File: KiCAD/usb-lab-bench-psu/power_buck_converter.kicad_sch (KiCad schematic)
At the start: 15 parts, among them U10 LMR16006X

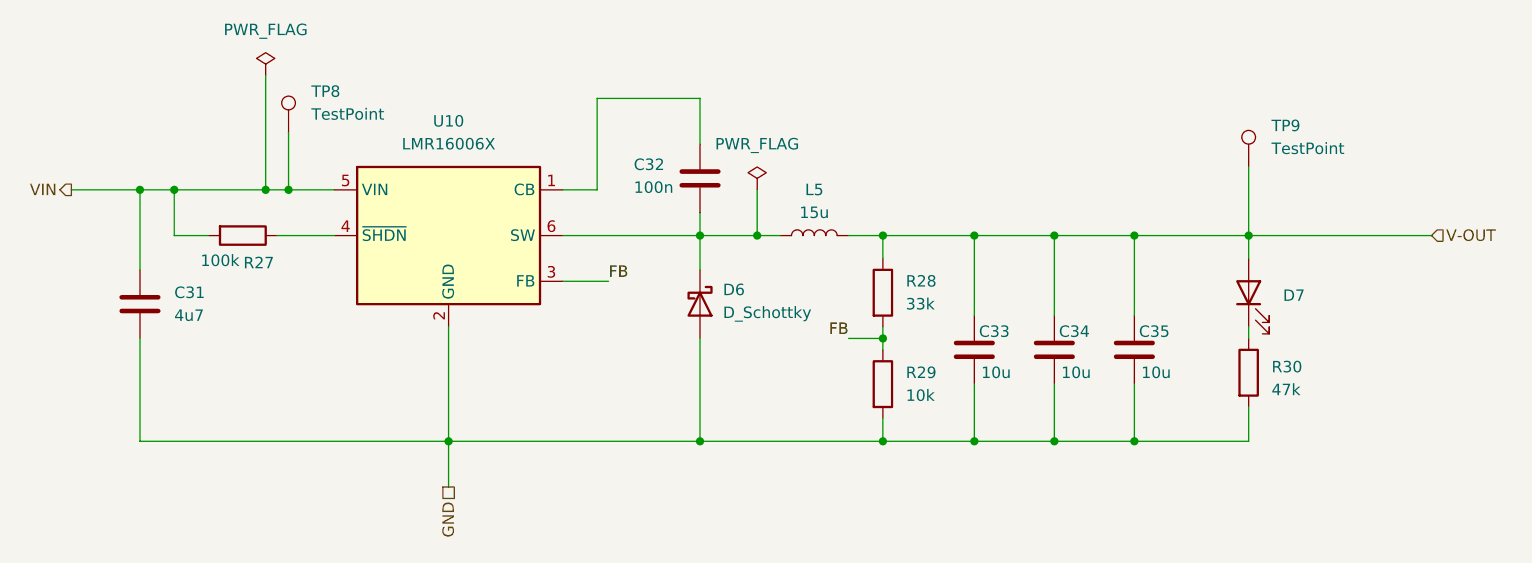
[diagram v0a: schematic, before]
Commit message: Fixed label directions
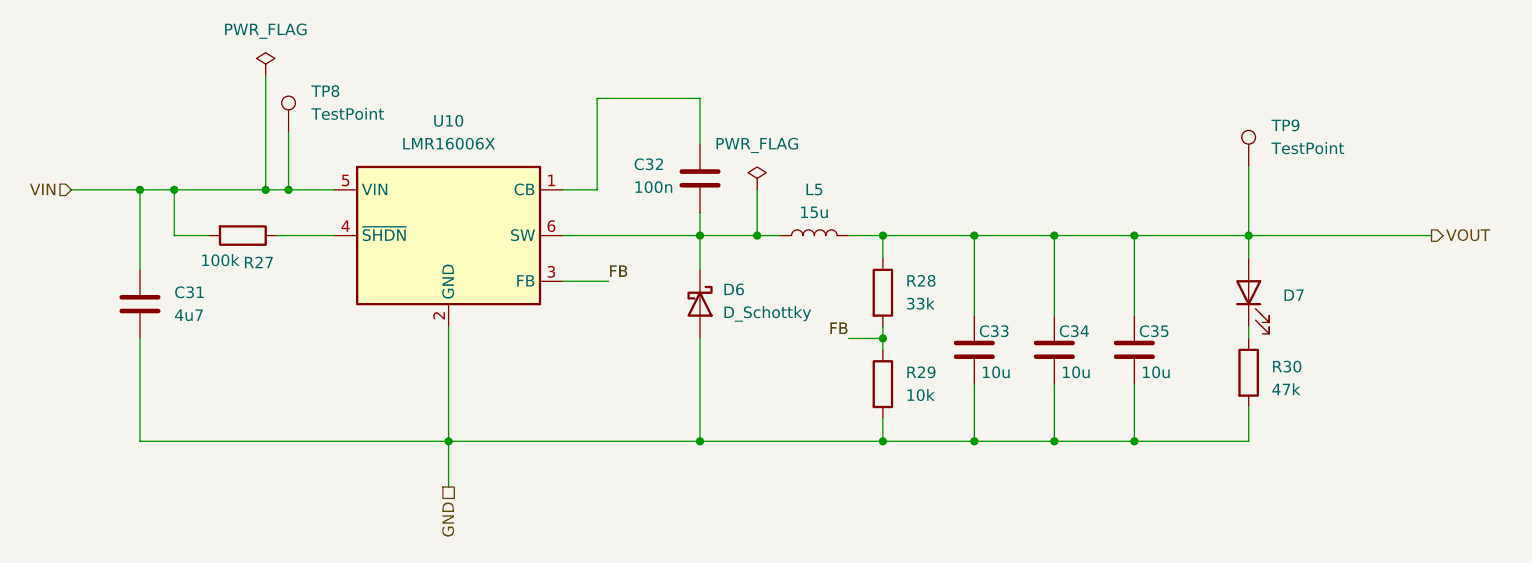
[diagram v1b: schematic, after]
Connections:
- net V-OUT renamed VOUT
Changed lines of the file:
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@@
 	)
 	(hierarchical_label "VIN"
-		(shape output)
+		(shape input)
 		(at 59.69 71.12 180)
 		(effects
@@
 		)
 	)
-	(hierarchical_label "V-OUT"
-		(shape input)
+	(hierarchical_label "VOUT"
+		(shape output)
 		(at 210.82 76.2 0)
 		(effects
@@
 					(unit 1)
 				)
-				(path "/63928bc9-e618-488a-a687-c6d5597f31d9/cc314cc1-26b0-4e6c-b14c-ea7785b99358/be63a1fd-c574-4431-a13c-219279271461"
-					(reference "C?")
-					(unit 1)
-				)
 			)
 		)
@@
 					(unit 1)
 				)
-				(path "/63928bc9-e618-488a-a687-c6d5597f31d9/cc314cc1-26b0-4e6c-b14c-ea7785b99358/be63a1fd-c574-4431-a13c-219279271461"
-					(reference "TP?")
-					(unit 1)
-				)
 			)
 		)
@@
 					(unit 1)
 				)
-				(path "/63928bc9-e618-488a-a687-c6d5597f31d9/cc314cc1-26b0-4e6c-b14c-ea7785b99358/be63a1fd-c574-4431-a13c-219279271461"
-					(reference "D?")
-					(unit 1)
-				)
 			)
 		)
@@
 					(unit 1)
 				)
-				(path "/63928bc9-e618-488a-a687-c6d5597f31d9/cc314cc1-26b0-4e6c-b14c-ea7785b99358/be63a1fd-c574-4431-a13c-219279271461"
-					(reference "#FLG?")
-					(unit 1)
-				)
 			)
 		)
@@
 					(unit 1)
 				)
-				(path "/63928bc9-e618-488a-a687-c6d5597f31d9/cc314cc1-26b0-4e6c-b14c-ea7785b99358/be63a1fd-c574-4431-a13c-219279271461"
-					(reference "R?")
-					(unit 1)
-				)
 			)
 		)
@@
 					(unit 1)
 				)
-				(path "/63928bc9-e618-488a-a687-c6d5597f31d9/cc314cc1-26b0-4e6c-b14c-ea7785b99358/be63a1fd-c574-4431-a13c-219279271461"
-					(reference "TP?")
-					(unit 1)
-				)
 			)
 		)
@@
 				(path "/63928bc9-e618-488a-a687-c6d5597f31d9/a793a91b-724b-4226-ba64-0dd946e3992c/ac711039-2592-4309-8412-c7dd8d2aeb8d"
 					(reference "C34")
-					(unit 1)
-				)
-				(path "/63928bc9-e618-488a-a687-c6d5597f31d9/cc314cc1-26b0-4e6c-b14c-ea7785b99358/be63a1fd-c574-4431-a13c-219279271461"
-					(reference "C?")
 					(unit 1)
 				)
@@
 					(unit 1)
 				)
-				(path "/63928bc9-e618-488a-a687-c6d5597f31d9/cc314cc1-26b0-4e6c-b14c-ea7785b99358/be63a1fd-c574-4431-a13c-219279271461"
-					(reference "R?")
-					(unit 1)
-				)
 			)
 		)
@@
 					(unit 1)
 				)
-				(path "/63928bc9-e618-488a-a687-c6d5597f31d9/cc314cc1-26b0-4e6c-b14c-ea7785b99358/be63a1fd-c574-4431-a13c-219279271461"
-					(reference "C?")
-					(unit 1)
-				)
 			)
 		)
@@
 				(path "/63928bc9-e618-488a-a687-c6d5597f31d9/a793a91b-724b-4226-ba64-0dd946e3992c/ac711039-2592-4309-8412-c7dd8d2aeb8d"
 					(reference "C32")
-					(unit 1)
-				)
-				(path "/63928bc9-e618-488a-a687-c6d5597f31d9/cc314cc1-26b0-4e6c-b14c-ea7785b99358/be63a1fd-c574-4431-a13c-219279271461"
-					(reference "C?")
 					(unit 1)
 				)
@@
 					(unit 1)
 				)
-				(path "/63928bc9-e618-488a-a687-c6d5597f31d9/cc314cc1-26b0-4e6c-b14c-ea7785b99358/be63a1fd-c574-4431-a13c-219279271461"
-					(reference "D?")
-					(unit 1)
-				)
 			)
 		)
@@
 					(unit 1)
 				)
-				(path "/63928bc9-e618-488a-a687-c6d5597f31d9/cc314cc1-26b0-4e6c-b14c-ea7785b99358/be63a1fd-c574-4431-a13c-219279271461"
-					(reference "R?")
-					(unit 1)
-				)
 			)
 		)
@@
 				(path "/63928bc9-e618-488a-a687-c6d5597f31d9/a793a91b-724b-4226-ba64-0dd946e3992c/ac711039-2592-4309-8412-c7dd8d2aeb8d"
 					(reference "C35")
-					(unit 1)
-				)
-				(path "/63928bc9-e618-488a-a687-c6d5597f31d9/cc314cc1-26b0-4e6c-b14c-ea7785b99358/be63a1fd-c574-4431-a13c-219279271461"
-					(reference "C?")
 					(unit 1)
 				)
@@
 					(unit 1)
 				)
-				(path "/63928bc9-e618-488a-a687-c6d5597f31d9/cc314cc1-26b0-4e6c-b14c-ea7785b99358/be63a1fd-c574-4431-a13c-219279271461"
-					(reference "#FLG?")
-					(unit 1)
-				)
 			)
 		)
@@
 				(path "/63928bc9-e618-488a-a687-c6d5597f31d9/a793a91b-724b-4226-ba64-0dd946e3992c/ac711039-2592-4309-8412-c7dd8d2aeb8d"
 					(reference "R27")
-					(unit 1)
-				)
-				(path "/63928bc9-e618-488a-a687-c6d5597f31d9/cc314cc1-26b0-4e6c-b14c-ea7785b99358/be63a1fd-c574-4431-a13c-219279271461"
-					(reference "R?")
 					(unit 1)
 				)
@@
 					(unit 1)
 				)
-				(path "/63928bc9-e618-488a-a687-c6d5597f31d9/cc314cc1-26b0-4e6c-b14c-ea7785b99358/be63a1fd-c574-4431-a13c-219279271461"
-					(reference "L?")
-					(unit 1)
-				)
 			)
 		)
@@
 					(unit 1)
 				)
-				(path "/63928bc9-e618-488a-a687-c6d5597f31d9/cc314cc1-26b0-4e6c-b14c-ea7785b99358/be63a1fd-c574-4431-a13c-219279271461"
-					(reference "U?")
-					(unit 1)
-				)
